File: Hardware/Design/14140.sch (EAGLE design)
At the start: 157 parts, among them J1 PST1,0/4-3,5, J10 PPPC101LFBN, J11 ICSP, J2 PST1,0&8-3,5, J3 PST1,0/3-3,5, J4 PST1,0/5-3,5, J5 PPPC101LFBN, J6 PPPC081LFBN, J7 PST1,0/6-3,5, J9 PPPC101LFBN, Q1 DMB, Q10 K84, Q11 K3N, Q12 K3N, Q13 K38, Q14 K3N, Q15 K3N, Q16 K3N, Q17 K3N, Q18 DMB, Q19 K38, Q2 K38, Q20 K1N, Q21 K38, Q22 K1N, Q23 K38, Q24 K1N, Q25 K38, Q26 K1N, Q27 K1N, Q28 K38, Q29 K1N, Q3 K1N, Q30 K38, Q31 K38, Q32 K1N, Q33 K3N, Q34 K3N, Q4 K1N, Q5 DMB, Q6 34N, Q7 K3N, Q8 K3N, Q9 K38, U1 LT3652, U2 I50115, U3 1087, U4 1087, U5 TPS3700, U6 ATMEGA328PB-AU, Y1 16MHz

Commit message: Eeprom: add uint16 and uint32 for use with solenoid
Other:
- note added: "AT DAY START U1 WILL SEND CURRENT THROUGH BODY DIODE OF Q5 UNTIL U5 B-SIDE HAS A CHANCE TO PULL DOWN GATE OF Q5"
- note added: "ONCE Q1 IS ON IT IS LATCHED BY Q2"
- note added: "ONCE Q5 IS ON THEN THE BATTERY AND U1 OUTPUT ARE CONNECTED. THE BATTERY CHARGES UP TO ABOUT 13.1V BEFORE THE U5 RELEASES PULL DOWN ON ITS A-SIDE TO TURN ON Q9 THAT PULLS DOWN ON Q1 GATE."
- note added: "Q2 LATCH RELEASES WHEN U5 B-SIDE OPENS"
- note added: "Q5 BATTERY DISCONNECT"
- note added: "Q6 BATTERY REVERSE PROTECTION"
- note removed: "BATTERY REVERSE PROTECTION"
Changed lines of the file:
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@@
 DOES NOT YET SUPPORT 328PB
 (iom328pb.h will show up with avr-libc when it does)</text>
-<text x="232.41" y="183.642" size="1.27" layer="98">BATTERY
+<text x="232.41" y="183.642" size="1.27" layer="98">Q6 BATTERY
 REVERSE
 PROTECTION</text>
@@
 IO2, 10K B=3380 CONN </text>
 <text x="320.294" y="32.004" size="1.778" layer="98">10/16/16</text>
+<text x="199.136" y="197.104" size="1.27" layer="98">Q5 BATTERY
+DISCONNECT</text>
+<text x="43.18" y="238.76" size="1.27" layer="98">AT DAY START U1 WILL SEND CURRENT THROUGH
+BODY DIODE OF Q5 UNTIL U5 B-SIDE HAS A
+CHANCE TO PULL DOWN GATE OF Q5</text>
+<text x="142.748" y="231.648" size="1.27" layer="98">ONCE Q5 IS ON THEN THE BATTERY AND U1 OUTPUT
+ARE CONNECTED. THE BATTERY CHARGES UP TO
+ABOUT 13.1V BEFORE THE U5 RELEASES PULL DOWN
+ON ITS A-SIDE TO TURN ON Q9 THAT PULLS DOWN
+ON Q1 GATE.</text>
+<text x="224.79" y="219.202" size="1.27" layer="98">ONCE Q1 IS
+ON IT IS
+LATCHED BY Q2</text>
+<text x="224.79" y="214.122" size="1.27" layer="98">Q2 LATCH RELEASES
+WHEN U5 B-SIDE OPENS</text>
 </plain>
 <instances>

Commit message: Hardware: ^6 review
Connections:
- removed net N$12: Q10.D, Q15.E, Q17.E, R39.2, R41.2
- removed net N$5: D1.A, J1.4.1
- new net CS_PWR: Q10.D, Q12.E, Q15.E, Q17.E, Q34.E, Q8.E, R16.2, R29.2, R39.2, R41.2, R58.2
- new net PV_RAW: D1.A, J1.4.1, R34.2
- net PV_IN: no longer R34.2
- net VIN: no longer Q12.E, Q34.E, Q8.E, R16.2, R29.2, R58.2
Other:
- note added: "1/16/17"
- note added: "ALL CS FROM CS_PWR ADC6 TO PV_RAW"
- note added: "CURRENT SOURCE PWR"
- note added: "HALL/VR FLOW SENSOR OR MT/HT/LT PULSE LOOP"
- note added: "^6"
- note removed: "1/4/16"
- note removed: "ADD BATTERY REVERSE PROTECTION"
- note removed: "CURRENT SOURCES FOR PULSE LOOP, HALL, OR VR"
- note removed: "^1"
- moved on the sheet: Q33, Q34, R58, R59

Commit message: SelfTest: not done yet but a good save point
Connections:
- net SHLD_VIN renamed VOUT
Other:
- note added: "VOUT"
- note removed: "VIN"
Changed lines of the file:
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@@
 <text x="362.204" y="116.332" size="1.27" layer="98">+3V3</text>
 <text x="362.204" y="111.252" size="1.27" layer="98">IOREF</text>
-<text x="362.204" y="126.492" size="1.27" layer="98">VIN</text>
+<text x="362.204" y="126.492" size="1.27" layer="98">VOUT</text>
 <text x="362.204" y="123.952" size="1.27" layer="98">GND</text>
 <text x="362.204" y="121.412" size="1.27" layer="98">GND</text>
@@
 </segment>
 </net>
-<net name="SHLD_VIN" class="0">
+<net name="VOUT" class="0">
 <segment>
 <pinref part="J6" gate="G$1" pin="1"/>

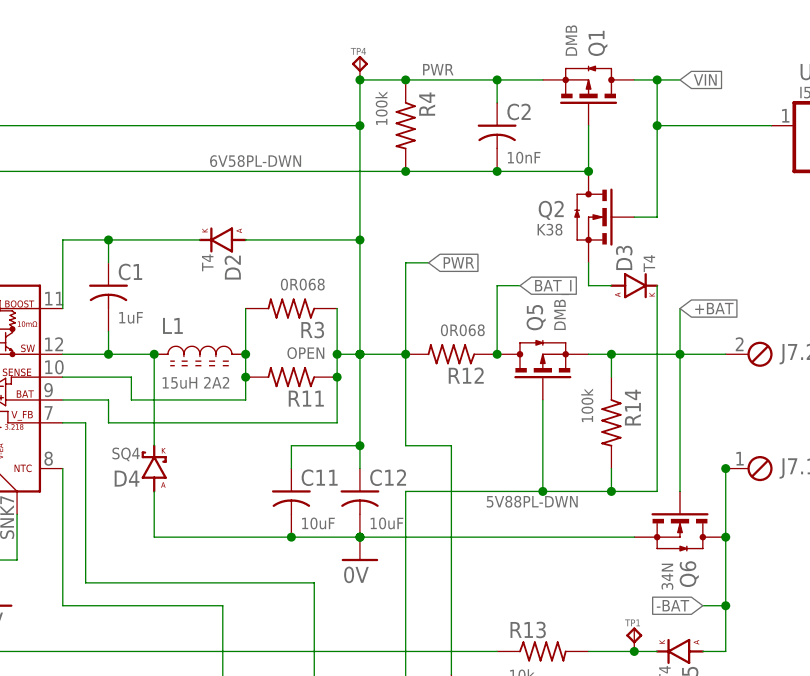
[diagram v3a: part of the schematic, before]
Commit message: Hardware: circuit node names for bat-discon and vin-discon
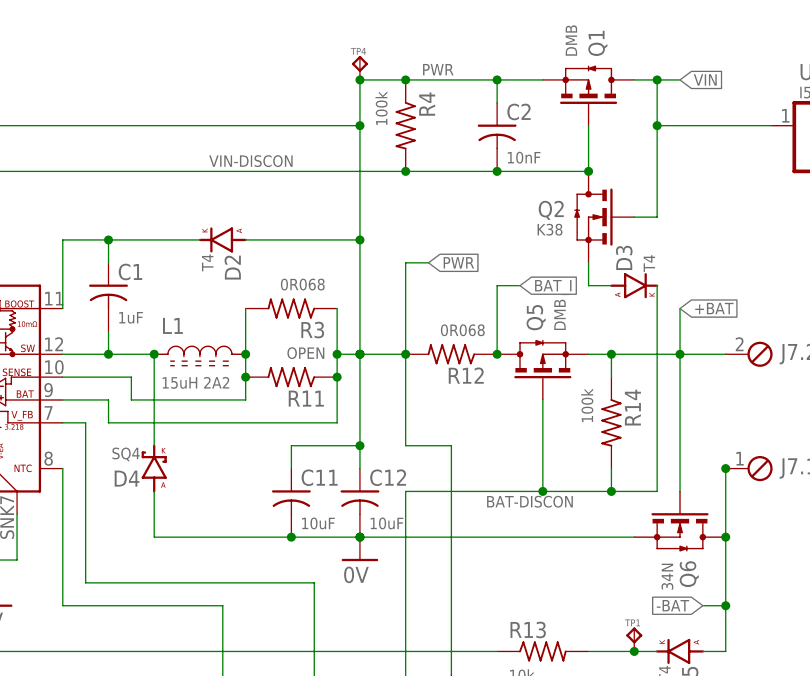
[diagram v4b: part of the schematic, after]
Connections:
- net 5V88PL-DWN renamed BAT-DISCON
- net 6V58PL-DWN renamed VIN-DISCON
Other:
- note added: "BATTERY DISCONNECT"
- note added: "BATTERY REVERSE PROTECTION"
- note added: "ONCE Q1 IS ON IT IS HELD BY Q2"
- note added: "Q2 RELEASES WHEN TPS3700 B-SIDE OPENS"
- note added: "VIN LATCH"
- note removed: "ONCE Q1 IS ON IT IS LATCHED BY Q2"
- note removed: "Q2 LATCH RELEASES WHEN U5 B-SIDE OPENS"
- note removed: "Q5 BATTERY DISCONNECT"
- note removed: "Q6 BATTERY REVERSE PROTECTION"
- note removed: "VOUT LATCH"
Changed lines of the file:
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@@
     NTC THERMISTOR
     0603 ON 0805 PAD</text>
-<text x="216.662" y="228.6" size="1.27" layer="98">VOUT
+<text x="216.662" y="228.6" size="1.27" layer="98">VIN
 LATCH</text>
 <text x="119.126" y="143.51" size="1.27" layer="98">DISCONNECT
@@
 DOES NOT YET SUPPORT 328PB
 (iom328pb.h will show up with avr-libc when it does)</text>
-<text x="232.41" y="183.642" size="1.27" layer="98">Q6 BATTERY
+<text x="232.41" y="183.642" size="1.27" layer="98">BATTERY
 REVERSE
 PROTECTION</text>
@@
 ADC6 TO PV_RAW</text>
 <text x="320.294" y="32.004" size="1.778" layer="98">1/16/17</text>
-<text x="199.136" y="197.104" size="1.27" layer="98">Q5 BATTERY
+<text x="199.898" y="198.628" size="1.27" layer="98">BATTERY
 DISCONNECT</text>
 <text x="43.18" y="238.76" size="1.27" layer="98">AT DAY START U1 WILL SEND CURRENT THROUGH
@@
 <text x="224.79" y="219.202" size="1.27" layer="98">ONCE Q1 IS
 ON IT IS
-LATCHED BY Q2</text>
-<text x="224.79" y="214.122" size="1.27" layer="98">Q2 LATCH RELEASES
-WHEN U5 B-SIDE OPENS</text>
+HELD BY Q2</text>
+<text x="224.79" y="214.122" size="1.27" layer="98">Q2  RELEASES WHEN
+TPS3700 B-SIDE OPENS</text>
 <text x="282.702" y="26.924" size="2.54" layer="98">^5</text>
 <text x="290.068" y="25.908" size="1.6764" layer="98">ADD 5V PLUG, PULL UP/DWN
@@
 </segment>
 </net>
-<net name="5V88PL-DWN" class="0">
+<net name="BAT-DISCON" class="0">
 <segment>
 <wire x1="210.82" y1="200.66" x2="210.82" y2="190.5" width="0.1524" layer="91"/>
@@
 </segment>
 </net>
-<net name="6V58PL-DWN" class="0">
+<net name="VIN-DISCON" class="0">
 <segment>
 <pinref part="Q2" gate="G$1" pin="D"/>

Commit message: Hardware: flow sensor info on schematic
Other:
- note added: "1k OHM"
- note added: "FLOW SENSOR"
- note added: "HALL/VR FLOW SENSOR OR MT/HT/LT SENSOR"
- note removed: "FT /W OC PULSE"
- note removed: "HALL/VR FLOW SENSOR OR MT/HT/LT PULSE LOOP"
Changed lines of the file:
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@@
 <text x="270.51" y="99.06" size="1.27" layer="98" rot="R90">17mA</text>
 <text x="291.084" y="104.14" size="1.27" layer="98" rot="R90">10mA</text>
-<wire x1="228.6" y1="91.44" x2="238.76" y2="91.44" width="0.1524" layer="98"/>
-<wire x1="238.76" y1="91.44" x2="238.76" y2="88.9" width="0.1524" layer="98"/>
-<wire x1="238.76" y1="88.9" x2="238.76" y2="78.74" width="0.1524" layer="98"/>
-<wire x1="238.76" y1="78.74" x2="238.76" y2="76.2" width="0.1524" layer="98"/>
-<wire x1="238.76" y1="76.2" x2="228.6" y2="76.2" width="0.1524" layer="98"/>
-<wire x1="228.6" y1="76.2" x2="228.6" y2="91.44" width="0.1524" layer="98"/>
-<text x="230.124" y="92.456" size="1.27" layer="98">FT /W OC PULSE</text>
-<text x="231.648" y="89.662" size="1.27" layer="98">RD</text>
-<text x="234.188" y="84.328" size="1.27" layer="98">WH</text>
-<text x="231.648" y="76.962" size="1.27" layer="98">BK</text>
-<wire x1="230.124" y1="87.884" x2="231.14" y2="87.884" width="0.1524" layer="98"/>
-<wire x1="231.14" y1="87.884" x2="233.172" y2="87.884" width="0.1524" layer="98"/>
-<wire x1="233.172" y1="87.884" x2="233.172" y2="81.534" width="0.1524" layer="98"/>
-<wire x1="233.172" y1="81.534" x2="233.172" y2="79.756" width="0.1524" layer="98"/>
-<wire x1="233.172" y1="79.756" x2="231.14" y2="79.756" width="0.1524" layer="98"/>
-<wire x1="231.14" y1="79.756" x2="230.124" y2="79.756" width="0.1524" layer="98"/>
-<wire x1="230.124" y1="79.756" x2="230.124" y2="87.884" width="0.1524" layer="98"/>
-<wire x1="235.458" y1="83.82" x2="235.458" y2="82.804" width="0.1524" layer="98"/>
-<wire x1="234.188" y1="82.55" x2="234.188" y2="82.042" width="0.1524" layer="98"/>
-<wire x1="234.188" y1="82.042" x2="234.188" y2="81.534" width="0.1524" layer="98"/>
-<wire x1="234.188" y1="81.534" x2="234.188" y2="81.026" width="0.1524" layer="98"/>
-<wire x1="234.188" y1="81.026" x2="234.188" y2="80.518" width="0.1524" layer="98"/>
-<wire x1="234.188" y1="82.042" x2="235.458" y2="82.804" width="0.1524" layer="98"/>
-<wire x1="235.458" y1="80.264" x2="234.188" y2="81.026" width="0.1524" layer="98"/>
-<wire x1="238.76" y1="78.74" x2="235.458" y2="78.74" width="0.1524" layer="98"/>
-<wire x1="235.458" y1="78.74" x2="231.14" y2="78.74" width="0.1524" layer="98"/>
-<wire x1="231.14" y1="78.74" x2="231.14" y2="79.756" width="0.1524" layer="98"/>
-<wire x1="238.76" y1="88.9" x2="231.14" y2="88.9" width="0.1524" layer="98"/>
-<wire x1="231.14" y1="88.9" x2="231.14" y2="87.884" width="0.1524" layer="98"/>
-<wire x1="235.458" y1="80.264" x2="235.458" y2="78.74" width="0.1524" layer="98"/>
-<wire x1="235.458" y1="80.264" x2="235.204" y2="80.772" width="0.1524" layer="98"/>
-<wire x1="235.458" y1="80.264" x2="234.95" y2="80.264" width="0.1524" layer="98"/>
-<wire x1="234.188" y1="81.534" x2="233.172" y2="81.534" width="0.1524" layer="98"/>
-<circle x="235.458" y="78.74" radius="0.254" width="0.381" layer="98"/>
-<text x="232.156" y="80.518" size="1.016" layer="98" rot="R90">VR | HALL</text>
-<wire x1="243.84" y1="83.82" x2="235.458" y2="83.82" width="0.1524" layer="98"/>
-<wire x1="243.84" y1="83.82" x2="243.84" y2="81.28" width="0.1524" layer="98"/>
-<wire x1="238.76" y1="78.74" x2="256.54" y2="78.74" width="0.1524" layer="98"/>
-<wire x1="256.54" y1="78.74" x2="256.54" y2="73.66" width="0.1524" layer="98"/>
-<wire x1="243.84" y1="81.28" x2="256.54" y2="81.28" width="0.1524" layer="98"/>
+<wire x1="223.52" y1="91.44" x2="233.68" y2="91.44" width="0.1524" layer="98"/>
+<wire x1="233.68" y1="91.44" x2="233.68" y2="88.9" width="0.1524" layer="98"/>
+<wire x1="233.68" y1="88.9" x2="233.68" y2="78.74" width="0.1524" layer="98"/>
+<wire x1="233.68" y1="78.74" x2="233.68" y2="76.2" width="0.1524" layer="98"/>
+<wire x1="233.68" y1="76.2" x2="223.52" y2="76.2" width="0.1524" layer="98"/>
+<wire x1="223.52" y1="76.2" x2="223.52" y2="91.44" width="0.1524" layer="98"/>
+<text x="225.044" y="92.456" size="1.27" layer="98">FLOW SENSOR</text>
+<text x="226.568" y="89.662" size="1.27" layer="98">RD</text>
+<text x="229.108" y="84.328" size="1.27" layer="98">WH</text>
+<text x="226.568" y="76.962" size="1.27" layer="98">BK</text>
+<wire x1="225.044" y1="87.884" x2="226.06" y2="87.884" width="0.1524" layer="98"/>
+<wire x1="226.06" y1="87.884" x2="228.092" y2="87.884" width="0.1524" layer="98"/>
+<wire x1="228.092" y1="87.884" x2="228.092" y2="81.534" width="0.1524" layer="98"/>
+<wire x1="228.092" y1="81.534" x2="228.092" y2="79.756" width="0.1524" layer="98"/>
+<wire x1="228.092" y1="79.756" x2="226.06" y2="79.756" width="0.1524" layer="98"/>
+<wire x1="226.06" y1="79.756" x2="225.044" y2="79.756" width="0.1524" layer="98"/>
+<wire x1="225.044" y1="79.756" x2="225.044" y2="87.884" width="0.1524" layer="98"/>
+<wire x1="230.378" y1="83.82" x2="230.378" y2="82.804" width="0.1524" layer="98"/>
+<wire x1="229.108" y1="82.55" x2="229.108" y2="82.042" width="0.1524" layer="98"/>
+<wire x1="229.108" y1="82.042" x2="229.108" y2="81.534" width="0.1524" layer="98"/>
+<wire x1="229.108" y1="81.534" x2="229.108" y2="81.026" width="0.1524" layer="98"/>
+<wire x1="229.108" y1="81.026" x2="229.108" y2="80.518" width="0.1524" layer="98"/>
+<wire x1="229.108" y1="82.042" x2="230.378" y2="82.804" width="0.1524" layer="98"/>
+<wire x1="230.378" y1="80.264" x2="229.108" y2="81.026" width="0.1524" layer="98"/>
+<wire x1="233.68" y1="78.74" x2="230.378" y2="78.74" width="0.1524" layer="98"/>
+<wire x1="230.378" y1="78.74" x2="226.06" y2="78.74" width="0.1524" layer="98"/>
+<wire x1="226.06" y1="78.74" x2="226.06" y2="79.756" width="0.1524" layer="98"/>
+<wire x1="233.68" y1="88.9" x2="226.06" y2="88.9" width="0.1524" layer="98"/>
+<wire x1="226.06" y1="88.9" x2="226.06" y2="87.884" width="0.1524" layer="98"/>
+<wire x1="230.378" y1="80.264" x2="230.378" y2="78.74" width="0.1524" layer="98"/>
+<wire x1="230.378" y1="80.264" x2="230.124" y2="80.772" width="0.1524" layer="98"/>
+<wire x1="230.378" y1="80.264" x2="229.87" y2="80.264" width="0.1524" layer="98"/>
+<wire x1="229.108" y1="81.534" x2="228.092" y2="81.534" width="0.1524" layer="98"/>
+<circle x="230.378" y="78.74" radius="0.254" width="0.381" layer="98"/>
+<text x="227.076" y="80.518" size="1.016" layer="98" rot="R90">VR | HALL</text>
+<wire x1="235.966" y1="83.82" x2="230.378" y2="83.82" width="0.1524" layer="98"/>
+<wire x1="233.68" y1="78.74" x2="236.22" y2="78.74" width="0.1524" layer="98"/>
+<wire x1="236.22" y1="81.28" x2="256.54" y2="81.28" width="0.1524" layer="98"/>
 <wire x1="256.54" y1="81.28" x2="256.54" y2="83.82" width="0.1524" layer="98"/>
-<wire x1="238.76" y1="88.9" x2="256.54" y2="88.9" width="0.1524" layer="98"/>
+<wire x1="233.68" y1="88.9" x2="241.3" y2="88.9" width="0.1524" layer="98"/>
+<wire x1="241.3" y1="88.9" x2="256.54" y2="88.9" width="0.1524" layer="98"/>
 <wire x1="256.54" y1="88.9" x2="256.54" y2="91.44" width="0.1524" layer="98"/>
 <text x="171.45" y="80.01" size="2.54" layer="98">DIGITAL
@@
 <text x="320.294" y="26.924" size="1.778" layer="98">10/16/16</text>
 <text x="219.71" y="94.996" size="2.54" layer="98">HALL/VR FLOW SENSOR OR
-MT/HT/LT PULSE LOOP</text>
+MT/HT/LT SENSOR</text>
+<wire x1="236.22" y1="81.28" x2="236.22" y2="78.74" width="0.1524" layer="98"/>
+<wire x1="235.966" y1="83.82" x2="236.474" y2="84.836" width="0.1524" layer="98"/>
+<wire x1="236.474" y1="84.836" x2="237.236" y2="82.804" width="0.1524" layer="98"/>
+<wire x1="237.998" y1="84.836" x2="237.236" y2="82.804" width="0.1524" layer="98"/>
+<wire x1="237.998" y1="84.836" x2="238.76" y2="82.804" width="0.1524" layer="98"/>
+<wire x1="239.522" y1="84.836" x2="238.76" y2="82.804" width="0.1524" layer="98"/>
+<wire x1="239.522" y1="84.836" x2="240.284" y2="82.804" width="0.1524" layer="98"/>
+<wire x1="240.792" y1="83.82" x2="240.284" y2="82.804" width="0.1524" layer="98"/>
+<wire x1="241.3" y1="83.82" x2="240.792" y2="83.82" width="0.1524" layer="98"/>
+<wire x1="241.3" y1="88.9" x2="241.3" y2="83.82" width="0.1524" layer="98"/>
+<circle x="241.3" y="88.9" radius="0.254" width="0.381" layer="98"/>
+<text x="234.442" y="85.852" size="1.27" layer="98">1k OHM</text>
 </plain>
 <instances>

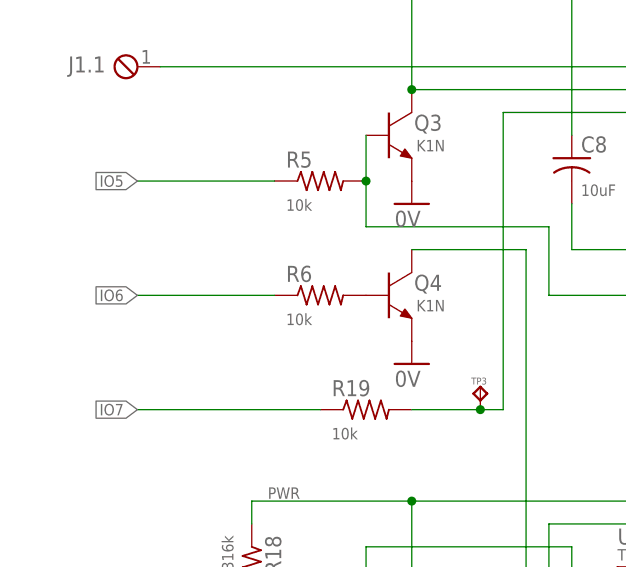
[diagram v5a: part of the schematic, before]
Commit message: Hardware: note on schematic about battery disconnect
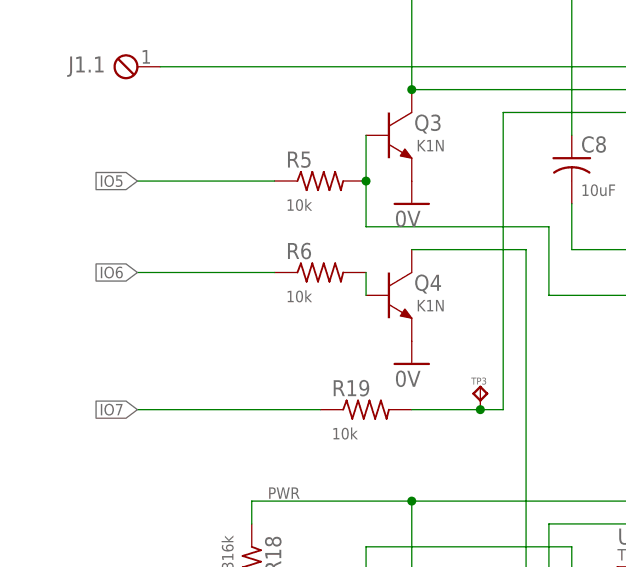
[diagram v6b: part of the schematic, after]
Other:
- note added: "NOTE: PV POWER WILL CONNECT THE BATTERY BUT THE MCU WILL EXPERIENCE A BROWN OUT SO DO NOT DISCONNECT DURING THE DAY."
- moved on the sheet: R6
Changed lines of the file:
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@@
 <text x="26.416" y="160.528" size="1.27" layer="98">OPEN COLLECTOR
 FAULT</text>
-<text x="22.86" y="173.482" size="1.27" layer="98">DISCONNECT
+<text x="22.86" y="176.022" size="1.27" layer="98">DISCONNECT
 BATTERY</text>
 <text x="119.126" y="133.35" size="1.27" layer="98">CONNECT
@@
 <circle x="241.3" y="88.9" radius="0.254" width="0.381" layer="98"/>
 <text x="234.442" y="85.852" size="1.27" layer="98">1k OHM</text>
+<text x="5.842" y="166.116" size="1.27" layer="98">NOTE: PV POWER WILL
+CONNECT THE BATTERY BUT THE MCU WILL
+EXPERIENCE A BROWN OUT SO DO NOT
+DISCONNECT DURING THE DAY.</text>
 </plain>
 <instances>
@@
 <instance part="R14" gate="G$1" x="218.44" y="198.12" rot="R270"/>
 <instance part="Q4" gate="G$1" x="50.8" y="172.72"/>
-<instance part="R6" gate="G$1" x="43.18" y="172.72"/>
+<instance part="R6" gate="G$1" x="43.18" y="175.26"/>
 <instance part="GND29" gate="1" x="53.34" y="165.1"/>
 <instance part="S1" gate="G$1" x="111.76" y="147.32" rot="R270"/>
@@
 <pinref part="R6" gate="G$1" pin="2"/>
 <pinref part="Q4" gate="G$1" pin="B"/>
+<wire x1="48.26" y1="175.26" x2="48.26" y2="172.72" width="0.1524" layer="91"/>
 </segment>
 </net>
@@
 </segment>
 <segment>
-<wire x1="22.86" y1="172.72" x2="38.1" y2="172.72" width="0.1524" layer="91"/>
-<label x="22.86" y="172.72" size="1.27" layer="91" rot="R180" xref="yes"/>
+<wire x1="22.86" y1="175.26" x2="38.1" y2="175.26" width="0.1524" layer="91"/>
+<label x="22.86" y="175.26" size="1.27" layer="91" rot="R180" xref="yes"/>
 <pinref part="R6" gate="G$1" pin="1"/>
 </segment>
